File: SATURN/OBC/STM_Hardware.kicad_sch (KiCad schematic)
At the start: 10 parts, among them J1 SWD Pins, J2 USB_OTG, U1 USBLC6-4SC6, U2 RV-3028-C7 32.768KHZ 1PPM-TA-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

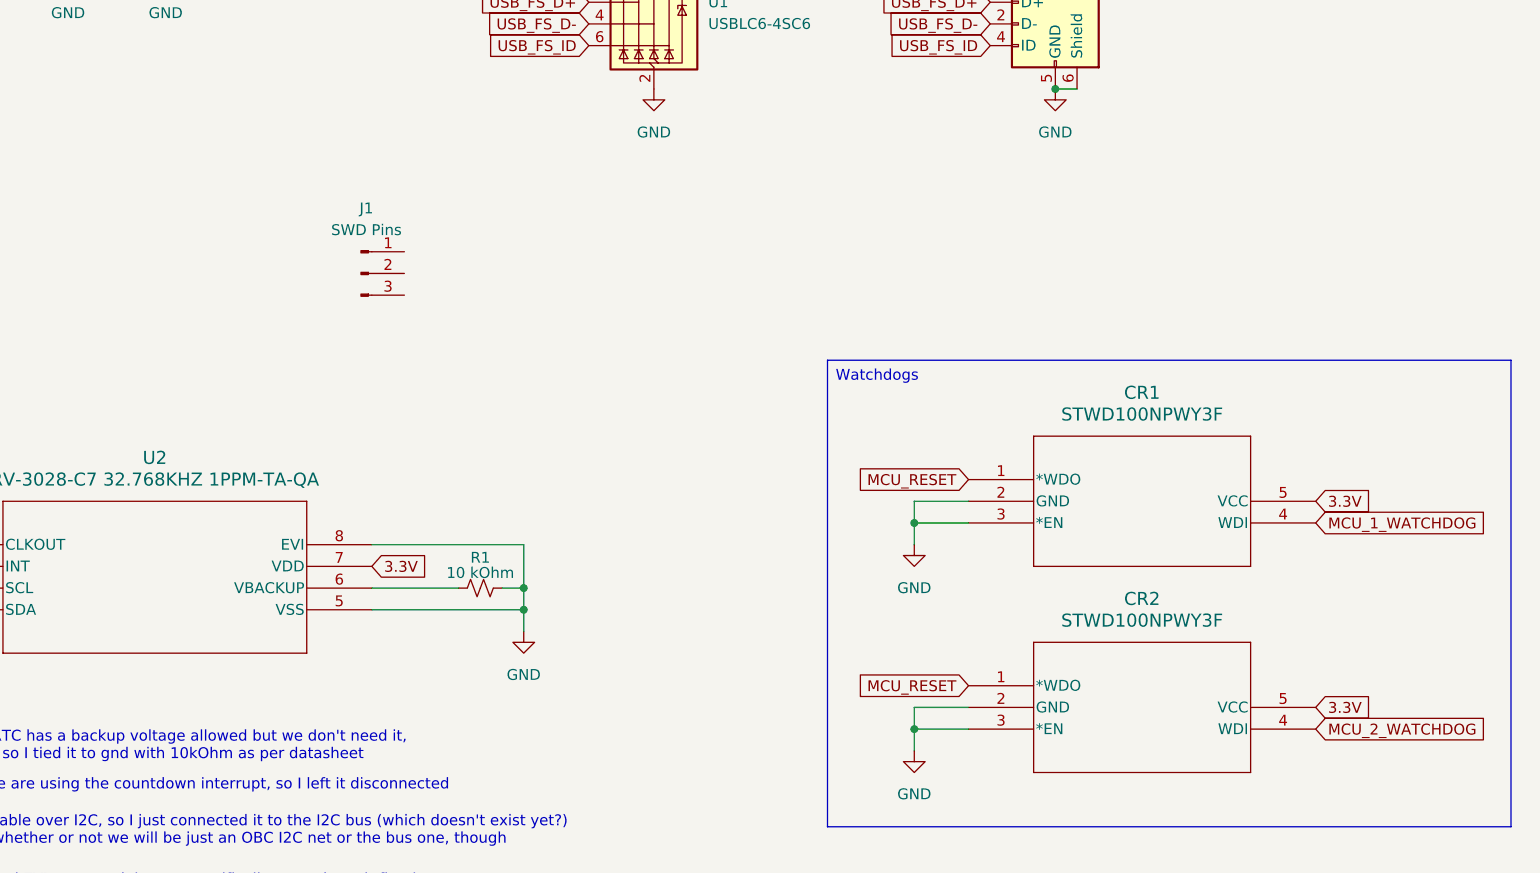
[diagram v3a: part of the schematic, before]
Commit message: Update SWD and 3.3V tags
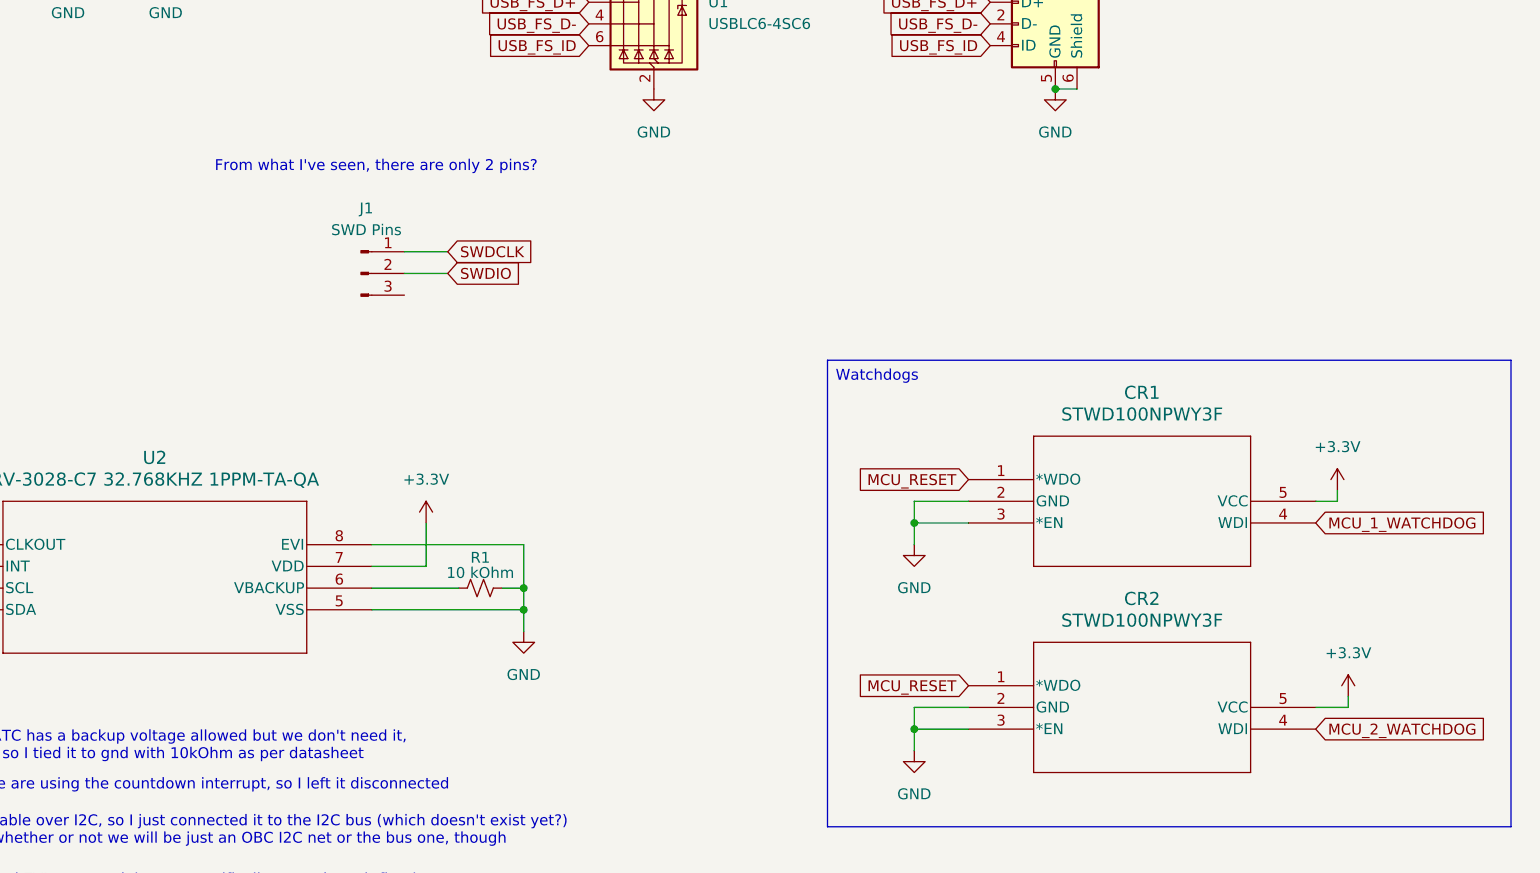
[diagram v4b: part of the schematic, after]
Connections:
- net SWDCLK: now reaches J1.1 (Pin_1)
- net SWDIO: now reaches J1.2 (Pin_2)
- net 3.3V renamed +3.3V
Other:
- note added: "From what I've seen, there are only 2 pins?"
